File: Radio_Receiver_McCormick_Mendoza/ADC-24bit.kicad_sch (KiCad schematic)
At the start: 14 parts, among them U12 PCM1808PWR

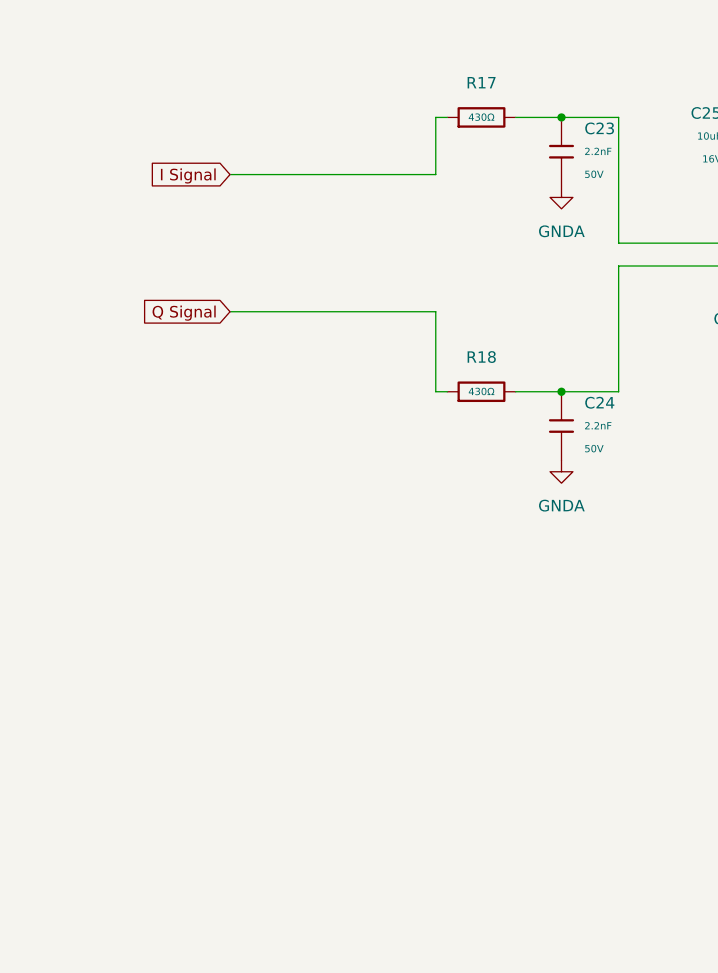
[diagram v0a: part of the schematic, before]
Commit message: Schematic connection edits
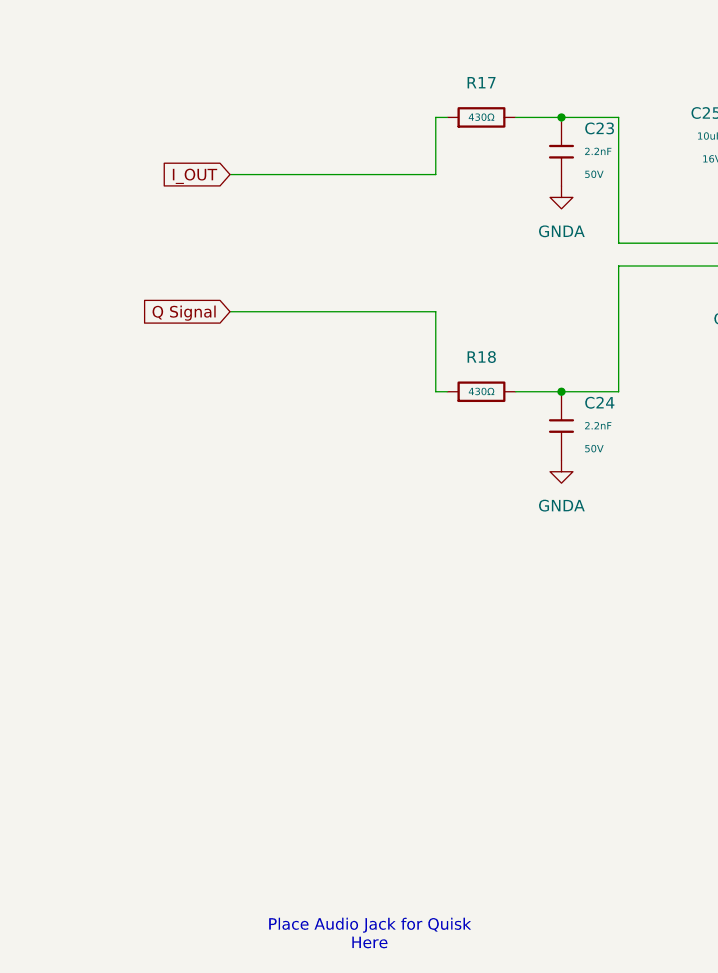
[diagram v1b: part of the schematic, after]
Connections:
- net I Signal renamed I_OUT
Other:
- note added: "Place Audio Jack for Quisk Here"
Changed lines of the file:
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@@
+		)
+	)
+	(text "Place Audio Jack for Quisk\nHere"
+		(exclude_from_sim no)
+		(at 92.964 159.512 0)
+		(effects
+			(font
+				(size 1.27 1.27)
+			)
 		)
 	)
@@
 		)
 	)
-	(global_label "I Signal"
+	(global_label "I_OUT"
 		(shape input)
 		(at 77.47 74.93 180)
@@
 		)
 		(property "Intersheetrefs" "${INTERSHEET_REFS}"
-			(at 66.9859 74.93 0)
+			(at 69.2838 74.93 0)
 			(hide yes)
 			(show_name no)

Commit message: Schematic edits power and signal systems
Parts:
- added C52: 100nF, PCM_JLCPCB:C_0805, symbol PCM_JLCPCB-Capacitors:0805,100nF
- added J21: SDR Out, Intro_to_CAD:Jack_3.5mm_CUI_SJ-3523-SMT_Horizontal, symbol Connector_Audio:AudioJack2_Ground
- added J22: Q_OUT, Connector_PinHeader_2.54mm:PinHeader_1x01_P2.54mm_Vertical, symbol Connector_Generic:Conn_01x01
- added J7: I_OUT, Connector_PinHeader_2.54mm:PinHeader_1x01_P2.54mm_Vertical, symbol Connector_Generic:Conn_01x01
- added R31: 10Ω, PCM_JLCPCB:R_0603, symbol PCM_JLCPCB-Resistors:0603,10Ω
- added e5: Groundloop_Insurance, Jumper:SolderJumper-2_P1.3mm_Bridged_RoundedPad1.0x1.5mm, symbol Jumper:Jumper_2_Bridged
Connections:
- net GND: now also C52.1, R31.2, e5.1 (A)
- net I_OUT: now also J21.R, J7.1 (Pin_1)
- net Q Signal renamed Q_OUT
- net Q_OUT: now also J21.T, J22.1 (Pin_1)
- net SKCI renamed SCKI
- new net: C52.2, J21.S, R31.1, e5.2 (B)
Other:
- note added: "GNDA?"
- moved on the sheet: C23

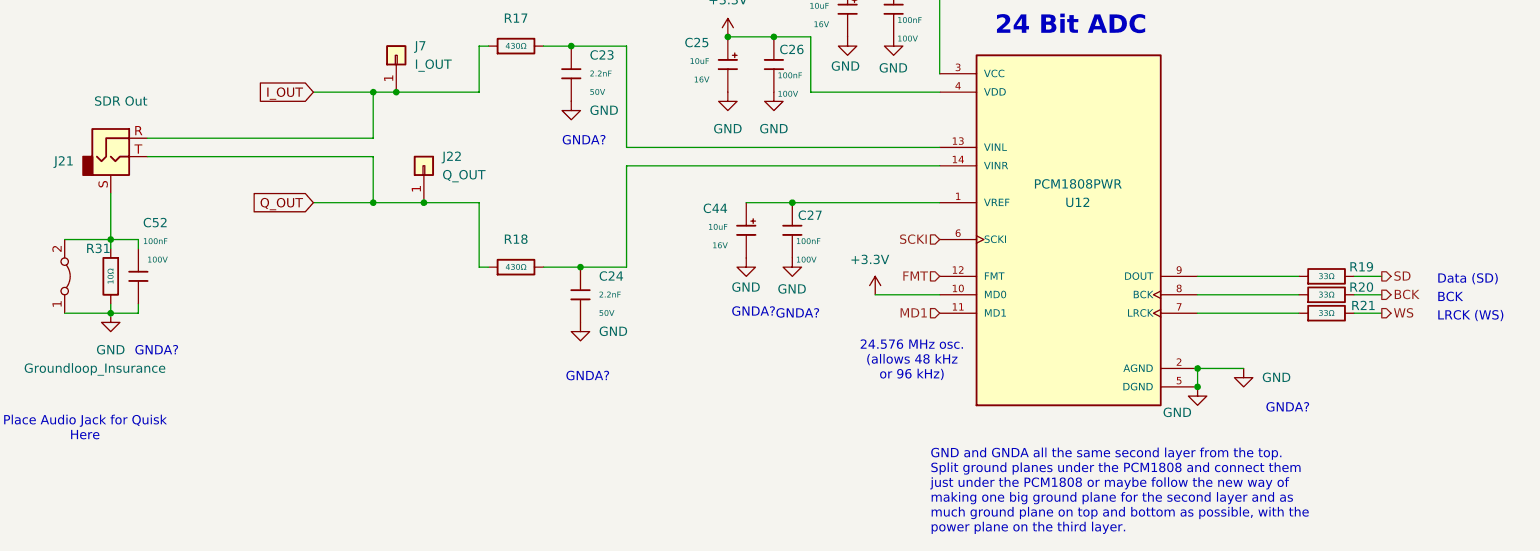
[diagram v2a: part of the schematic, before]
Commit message: Added bibliography source and schematic edits
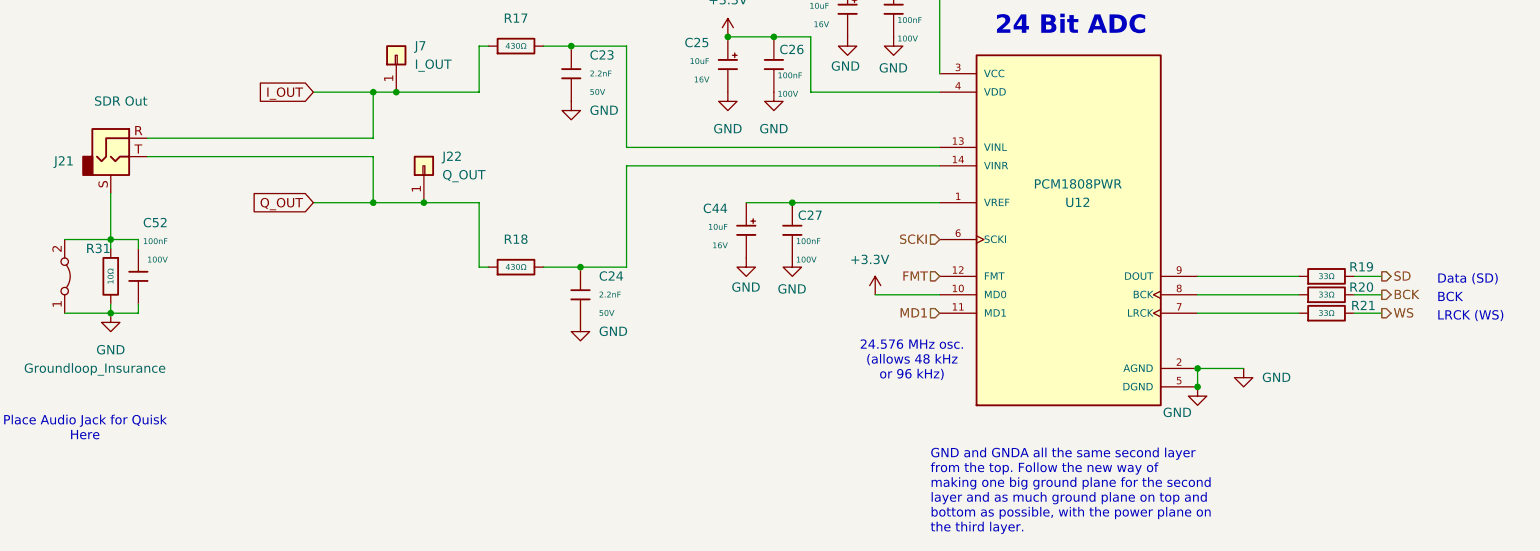
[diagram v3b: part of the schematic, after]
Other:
- note added: "GND and GNDA all the same second layer from the top. Follow the new way of making one big ground plane for the second layer and as much ground plane on top and bottom as possible, with the power plane on the third layer."
- note removed: "GND and GNDA all the same second layer from the top. Split ground planes under the PCM1808 and connect them just under the PCM1808 or maybe follow the new way of making one big ground plane for the second layer and as much ground plane on top and bottom as possible, with the power plane on the third layer."
- note removed: "GNDA?"
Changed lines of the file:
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@@
 		(comment 3 "Jeffrey McCormick")
 	)
-	(text "GND and GNDA all the same second layer from the top.\nSplit ground planes under the PCM1808 and connect them\njust under the PCM1808 or maybe follow the new way of\nmaking one big ground plane for the second layer and as\nmuch ground plane on top and bottom as possible, with the\npower plane on the third layer."
+	(text "GND and GNDA all the same second layer \nfrom the top. Follow the new way of\nmaking one big ground plane for the second\nlayer and as much ground plane on top and \nbottom as possible, with the power plane on\nthe third layer."
 		(exclude_from_sim no)
 		(at 162.56 135.89 0)
@@
 			)
 			(justify left bottom)
-		)
-	)
-	(text "GNDA?"
-		(exclude_from_sim no)
-		(at 144.272 105.664 0)
-		(effects
-			(font
-				(size 1.27 1.27)
-			)
-		)
-	)
-	(text "GNDA?"
-		(exclude_from_sim no)
-		(at 211.836 118.618 0)
-		(effects
-			(font
-				(size 1.27 1.27)
-			)
-		)
-	)
-	(text "GNDA?"
-		(exclude_from_sim no)
-		(at 138.176 105.41 0)
-		(effects
-			(font
-				(size 1.27 1.27)
-			)
-		)
-	)
-	(text "GNDA?"
-		(exclude_from_sim no)
-		(at 55.88 110.744 0)
-		(effects
-			(font
-				(size 1.27 1.27)
-			)
 		)
 	)
@@
 			)
 			(justify left bottom)
-		)
-	)
-	(text "GNDA?"
-		(exclude_from_sim no)
-		(at 115.316 114.3 0)
-		(effects
-			(font
-				(size 1.27 1.27)
-			)
 		)
 	)
@@
 		(effects
 			(font
-				(size 1.27 1.27)
-			)
-		)
-	)
-	(text "GNDA?"
-		(exclude_from_sim no)
-		(at 114.808 81.788 0)
-		(effects
-			(font

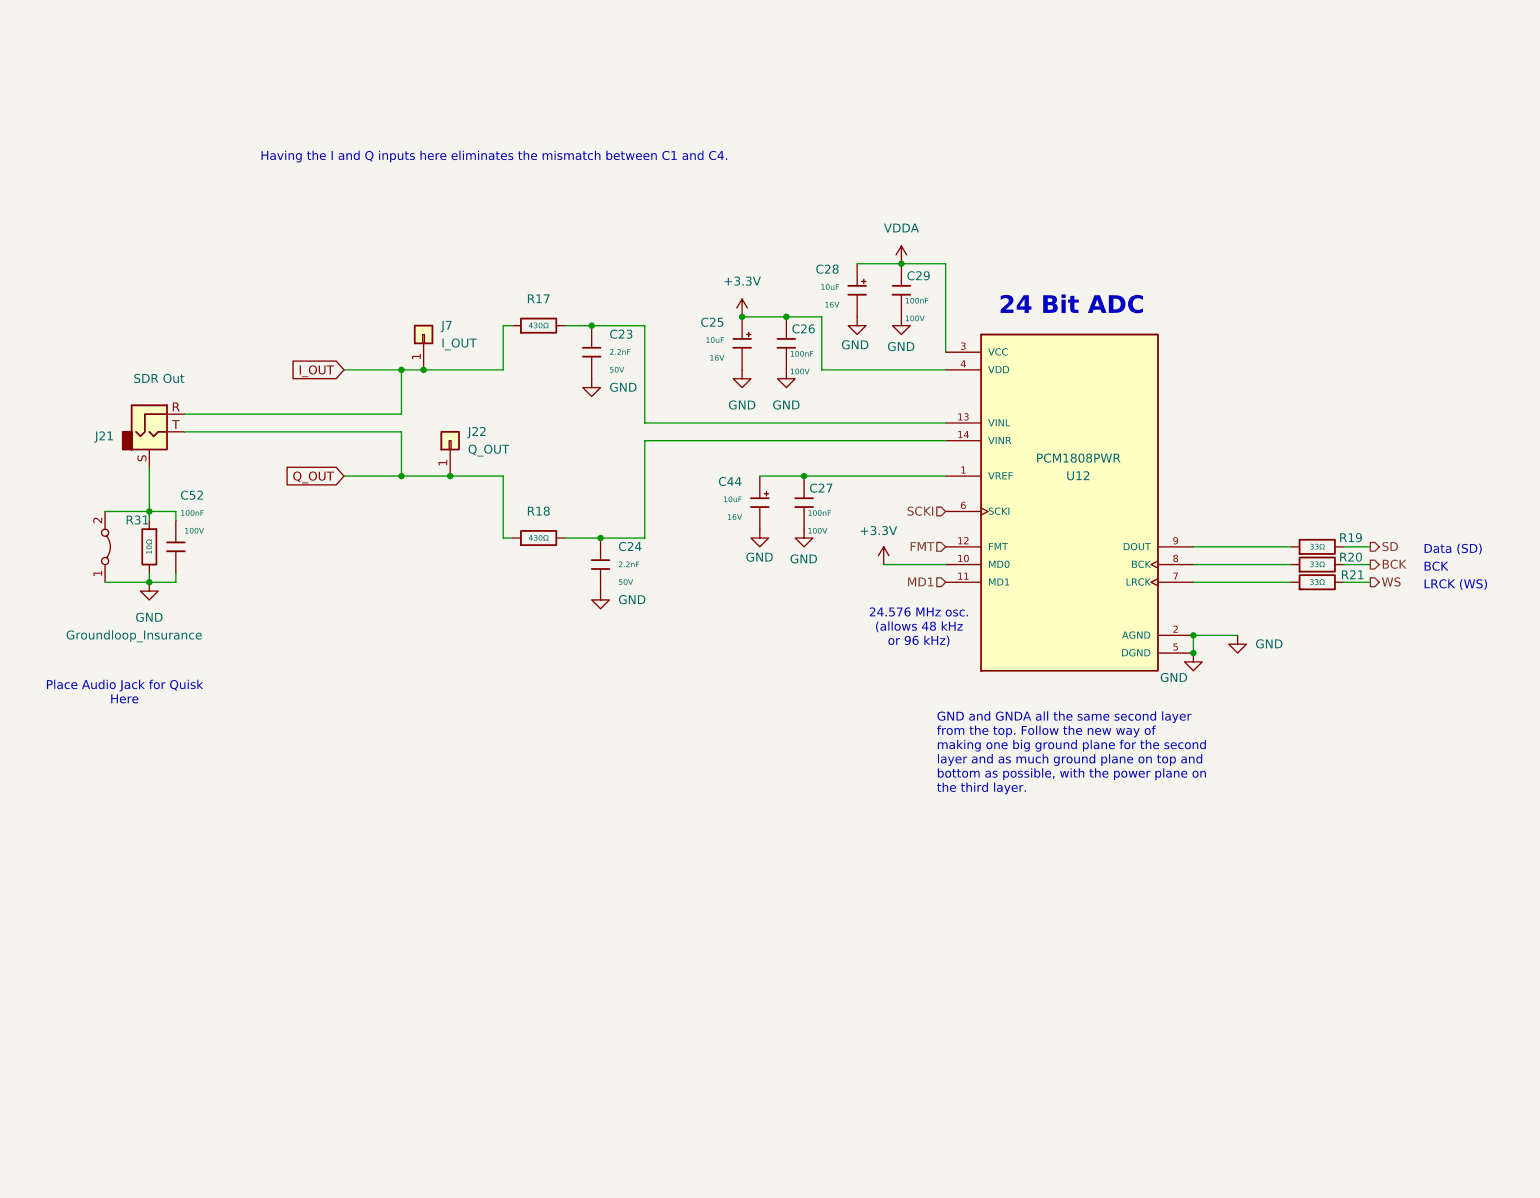
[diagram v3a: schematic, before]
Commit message: Added reference voltage stability by buffer amp
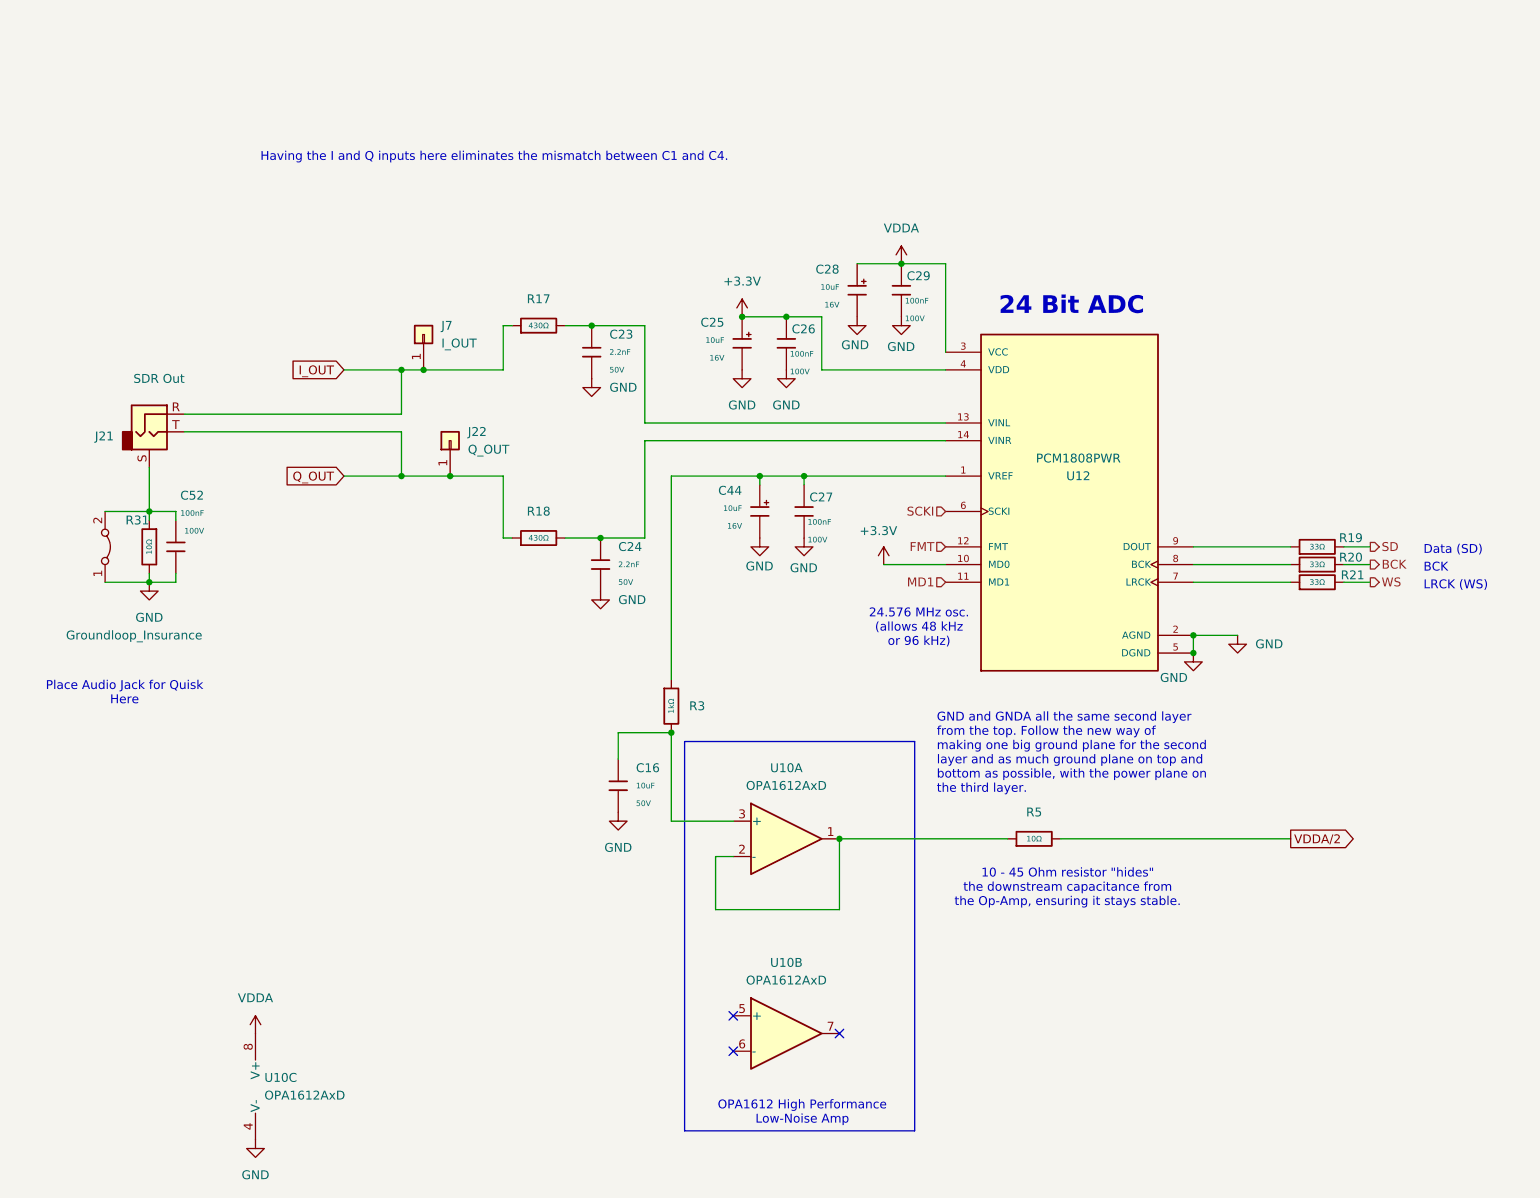
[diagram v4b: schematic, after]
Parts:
- added C16: 10uF, PCM_JLCPCB:C_0805, symbol PCM_JLCPCB-Capacitors:0805,10uF,(2)
- added R3: 1kΩ, PCM_JLCPCB:R_0402, symbol PCM_JLCPCB-Resistors:0402,1kΩ
- added R5: 10Ω, PCM_JLCPCB:R_0805, symbol PCM_JLCPCB-Resistors:0805,10Ω
- added U10: OPA1612AxD, symbol Amplifier_Operational:OPA1612AxD
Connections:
- net GND: now also C16.2, U10.4 (V-)
- net VDDA: now also U10.8 (V+)
- net at C27.2, C44.1, U12.1 (VREF): now also R3.1
- new net: C16.1, R3.2, U10.3 (+)
- new net: R5.1, U10.1, U10.2 (-)
- new net VDDA/2: R5.2
- no-connect marks 0 -> 3
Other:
- note added: "10 - 45 Ohm resistor "hides" the downstream capacitance from the Op-Amp, ensuring it stays stable."
- note added: "OPA1612 High Performance Low-Noise Amp"
- moved on the sheet: C27, C44
